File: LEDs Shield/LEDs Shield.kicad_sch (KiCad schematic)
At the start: 1 part, among them J3 LEDs and GND

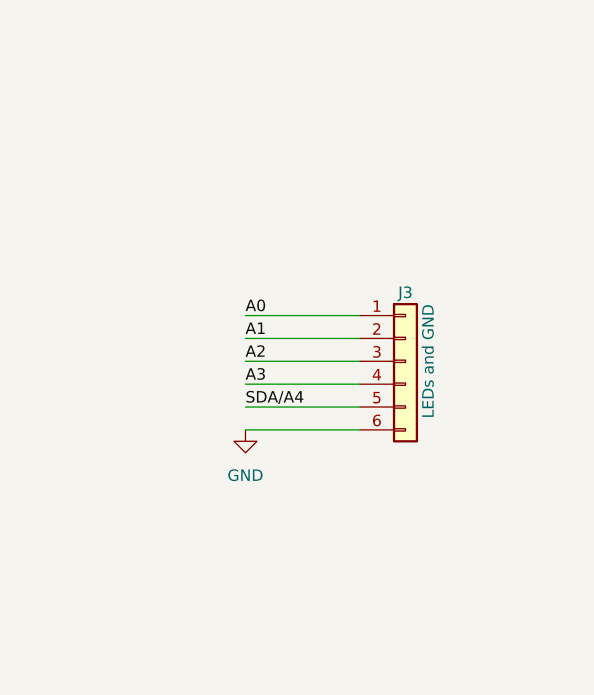
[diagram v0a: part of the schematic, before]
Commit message: Added support for management server, implemented an ipython client
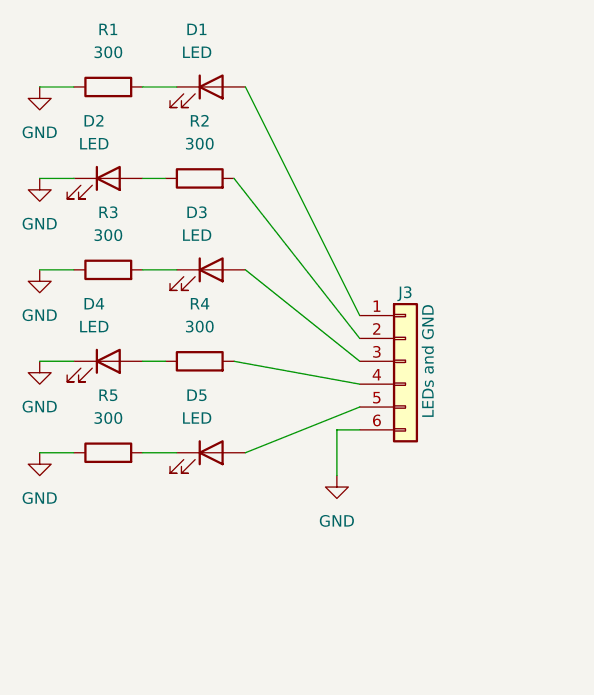
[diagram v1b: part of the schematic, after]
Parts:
- added D1, D2, D3, D4, D5: LED, LED_THT:LED_D3.0mm, symbol Device:LED
- added R1, R2, R3, R4, R5: 300, Resistor_SMD:R_0603_1608Metric_Pad0.98x0.95mm_HandSolder, symbol Device:R
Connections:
- net GND: now also D2.1 (K), D4.1 (K), R1.1, R3.1, R5.1
- net A0: no longer names the net of J3.1 (Pin_1)
- net A0: now also D1.2 (A)
- net A1: no longer names the net of J3.2 (Pin_2)
- net A1: now also R2.2
- net A2: no longer names the net of J3.3 (Pin_3)
- net A2: now also D3.2 (A)
- net A3: no longer names the net of J3.4 (Pin_4)
- net A3: now also R4.2
- net SDA/A4: no longer names the net of J3.5 (Pin_5)
- net SDA/A4: now also D5.2 (A)
- new net: D5.1 (K), R5.2
- new net: D2.2 (A), R2.1
- new net: D1.1 (K), R1.2
- new net: D4.2 (A), R4.1
- new net: D3.1 (K), R3.2
